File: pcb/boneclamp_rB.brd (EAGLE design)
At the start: 160 x 100 mm, 70 parts, among them IC1 24C, U1 AD8032ARZ-REEL7, U2 LT1964ES5-5TRMPBF, U4 TLV70245DBVT, U7 AD7682BCPZ, U8 TPS63700DRCT, U9 ADA4841-2YRZ

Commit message: Minor fixed to EEPROM circuit and ADC VREF buffer. Stephano, don't kill me.
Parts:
- removed S1: SWS002, smd-special:SMS-002
- removed SJ5: (no value), jumper:SJ
- added C2: 0.1uF, rcl:C0805
- added JP1: (no value), jumper:JP1
- added S2: SWS003, smd-special:SMS-003
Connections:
- net N$12 renamed ADC_CNV
- net AGND: now also C2.2
- net DGND: now also S2.4, S2.5, S2.6; no longer S1.3, S1.4
- net N$14: now also S2.1; no longer R8.1, S1.1
- net N$18: now also R8.1, S2.2; no longer S1.2
- net N$19: now also S2.3
- net N$21: now also JP1.2; no longer SJ5.1
- net N$22: now also JP1.1; no longer SJ5.2
- net VDD: now also C2.1
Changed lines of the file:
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@@
 <element name="SJ4" library="jumper" package="SJ" value="" x="25.4" y="58.42" rot="R90"/>
 <element name="IC1" library="on-semiconductor-01" package="SO-08" value="24C" x="25.4" y="27.94"/>
-<element name="S1" library="smd-special" package="SMS-002" value="SWS002" x="15.24" y="41.91"/>
 <element name="C22" library="rcl" package="C0603" value="0.1uF" x="12.7" y="24.13"/>
 <element name="R6" library="rcl" package="R0603" value="5.6k" x="12.7" y="20.32"/>
@@
 <element name="R10" library="rcl" package="R0603" value="5.6k" x="12.7" y="0"/>
 <element name="R11" library="rcl" package="R0603" value="10k" x="12.7" y="-5.08"/>
-<element name="SJ5" library="jumper" package="SJ" value="" x="12.7" y="-11.43"/>
 <element name="U$42" library="analog-devices-02" package="MO-153-AB" value="AD5686" x="17.78" y="60.96"/>
 <element name="U7" library="analog-devices-02" package="QFN50P400X400X100-21N" value="AD7682BCPZ" x="36.83" y="60.96">
@@
 <element name="SJ7" library="jumper" package="SJ" value="" x="-111.76" y="-334.01"/>
 <element name="SJ8" library="jumper" package="SJ" value="" x="-111.76" y="-339.09"/>
+<element name="JP1" library="jumper" package="JP1" value="" x="-118.11" y="-336.55"/>
+<element name="S2" library="smd-special" package="SMS-003" value="SWS003" x="-114.3" y="-346.71"/>
+<element name="C2" library="rcl" package="C0805" value="0.1uF" x="-119.38" y="-355.6"/>
 </elements>
 <signals>
@@
 <contactref element="U7" pad="20"/>
 <contactref element="U1" pad="8"/>
+<contactref element="C2" pad="1"/>
+<wire x1="-108.0262" y1="-302.895" x2="-120.33" y2="-355.6" width="0" layer="19" extent="1-1"/>
 <wire x1="-84.77" y1="-285.75" x2="-108.0262" y2="-302.895" width="0" layer="19" extent="1-1"/>
 <wire x1="-84.77" y1="-236.22" x2="-84.77" y2="-285.75" width="0" layer="19" extent="1-1"/>
@@
 <contactref element="U$42" pad="9"/>
 <contactref element="U$42" pad="16"/>
+<contactref element="C2" pad="2"/>
 <wire x1="-82.87" y1="-177.8" x2="-83.7692" y2="-167.9702" width="0" layer="19" extent="1-1"/>
 <wire x1="-82.87" y1="-184.15" x2="-82.87" y2="-177.8" width="0" layer="19" extent="1-1"/>
@@
 <wire x1="-110.81" y1="-314.96" x2="-112.9538" y2="-306.705" width="0" layer="19" extent="1-1"/>
 <wire x1="-110.91" y1="-327.66" x2="-110.81" y2="-314.96" width="0" layer="19" extent="1-1"/>
+<wire x1="-118.43" y1="-355.6" x2="-110.91" y2="-327.66" width="0" layer="19" extent="1-1"/>
 <wire x1="1.905" y1="19.05" x2="-81.0768" y2="-61.468" width="0" layer="19" extent="1-1"/>
 <wire x1="4.445" y1="19.05" x2="1.905" y2="19.05" width="0" layer="19" extent="1-1"/>
@@
 <contactref element="C22" pad="2"/>
 <contactref element="IC1" pad="4"/>
-<contactref element="S1" pad="3"/>
-<contactref element="S1" pad="4"/>
-<wire x1="25.4" y1="59.182" x2="50.165" y2="74.93" width="0" layer="19" extent="1-1"/>
-<wire x1="16.51" y1="46.4058" x2="25.4" y2="59.182" width="0" layer="19" extent="1-1"/>
-<wire x1="13.97" y1="46.4058" x2="16.51" y2="46.4058" width="0" layer="19" extent="1-1"/>
-<wire x1="13.55" y1="24.13" x2="13.97" y2="46.4058" width="0" layer="19" extent="1-1"/>
+<contactref element="S2" pad="5"/>
+<contactref element="S2" pad="6"/>
+<contactref element="S2" pad="4"/>
+<wire x1="-114.3" y1="-342.2142" x2="-116.84" y2="-342.2142" width="0" layer="19" extent="1-1"/>
+<wire x1="-111.76" y1="-342.2142" x2="-114.3" y2="-342.2142" width="0" layer="19" extent="1-1"/>
+<wire x1="13.55" y1="24.13" x2="-111.76" y2="-342.2142" width="0" layer="19" extent="1-1"/>
 <wire x1="27.305" y1="25.34" x2="13.55" y2="24.13" width="0" layer="19" extent="1-1"/>
+<wire x1="25.4" y1="59.182" x2="27.305" y2="25.34" width="0" layer="19" extent="1-1"/>
+<wire x1="50.165" y1="74.93" x2="25.4" y2="59.182" width="0" layer="19" extent="1-1"/>
 </signal>
 <signal name="VSS">
@@
 </signal>
 <signal name="N$14">
-<contactref element="S1" pad="1"/>
 <contactref element="IC1" pad="1"/>
 <contactref element="R7" pad="1"/>
-<contactref element="R8" pad="1"/>
-<wire x1="11.85" y1="15.24" x2="11.85" y2="10.16" width="0" layer="19" extent="1-1"/>
-<wire x1="13.97" y1="37.4142" x2="11.85" y2="15.24" width="0" layer="19" extent="1-1"/>
-<wire x1="23.495" y1="25.34" x2="13.97" y2="37.4142" width="0" layer="19" extent="1-1"/>
+<contactref element="S2" pad="1"/>
+<wire x1="11.85" y1="15.24" x2="-116.84" y2="-351.2058" width="0" layer="19" extent="1-1"/>
+<wire x1="23.495" y1="25.34" x2="11.85" y2="15.24" width="0" layer="19" extent="1-1"/>
 </signal>
 <signal name="N$18">
 <contactref element="IC1" pad="2"/>
-<contactref element="S1" pad="2"/>
-<wire x1="24.765" y1="25.34" x2="16.51" y2="37.4142" width="0" layer="19" extent="1-1"/>
+<contactref element="S2" pad="2"/>
+<contactref element="R8" pad="1"/>
+<wire x1="11.85" y1="10.16" x2="-114.3" y2="-351.2058" width="0" layer="19" extent="1-1"/>
+<wire x1="24.765" y1="25.34" x2="11.85" y2="10.16" width="0" layer="19" extent="1-1"/>
 </signal>
 <signal name="N$19">
 <contactref element="IC1" pad="3"/>
 <contactref element="R9" pad="1"/>
+<contactref element="S2" pad="3"/>
+<wire x1="11.85" y1="5.08" x2="-111.76" y2="-351.2058" width="0" layer="19" extent="1-1"/>
 <wire x1="26.035" y1="25.34" x2="11.85" y2="5.08" width="0" layer="19" extent="1-1"/>
 </signal>
 <signal name="N$22">
 <contactref element="R11" pad="1"/>
-<contactref element="SJ5" pad="2"/>
-<wire x1="11.85" y1="-5.08" x2="13.462" y2="-11.43" width="0" layer="19" extent="1-1"/>
+<contactref element="JP1" pad="1"/>
+<wire x1="11.85" y1="-5.08" x2="-118.11" y2="-337.82" width="0" layer="19" extent="1-1"/>
 </signal>
 <signal name="N$21">
-<contactref element="SJ5" pad="1"/>
 <contactref element="IC1" pad="7"/>
-<wire x1="24.765" y1="30.54" x2="11.938" y2="-11.43" width="0" layer="19" extent="1-1"/>
+<contactref element="JP1" pad="2"/>
+<wire x1="24.765" y1="30.54" x2="-118.11" y2="-335.28" width="0" layer="19" extent="1-1"/>
 </signal>
 <signal name="SYS_5V">
@@
 <wire x1="38.608" y1="60.452" x2="-110.998" y2="-334.01" width="0" layer="19" extent="1-1"/>
 </signal>
-<signal name="N$12">
+<signal name="ADC_CNV">
 <contactref element="U7" pad="11"/>
 </signal>

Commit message: Minor edit
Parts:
- added TP7: TPB1,27, testpad:B1,27
- moved JP1 420.5 mm to (127.0, 5.08)
- moved S2 408.9 mm to (114.3, -7.62)
- moved TP6 316.4 mm to (157.5, -10.2)
- moved TP5 315.0 mm to (152.4, -1.27)
- moved C22 127.0 mm to (139.7, 24.1)
- moved R10 127.0 mm to (139.7, 0.00)
- moved R11 127.0 mm to (139.7, -5.08)
- moved R6 127.0 mm to (139.7, 20.3)
- moved R7 127.0 mm to (139.7, 15.2)
- moved R8 127.0 mm to (139.7, 10.2)
- moved R9 127.0 mm to (139.7, 5.08)
- moved IC1 95.7 mm to (120.7, 19.1)
- moved C12 40.9 mm to (-47.0, -261.6)
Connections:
- net I2C2_SDA: now also TP7.TP

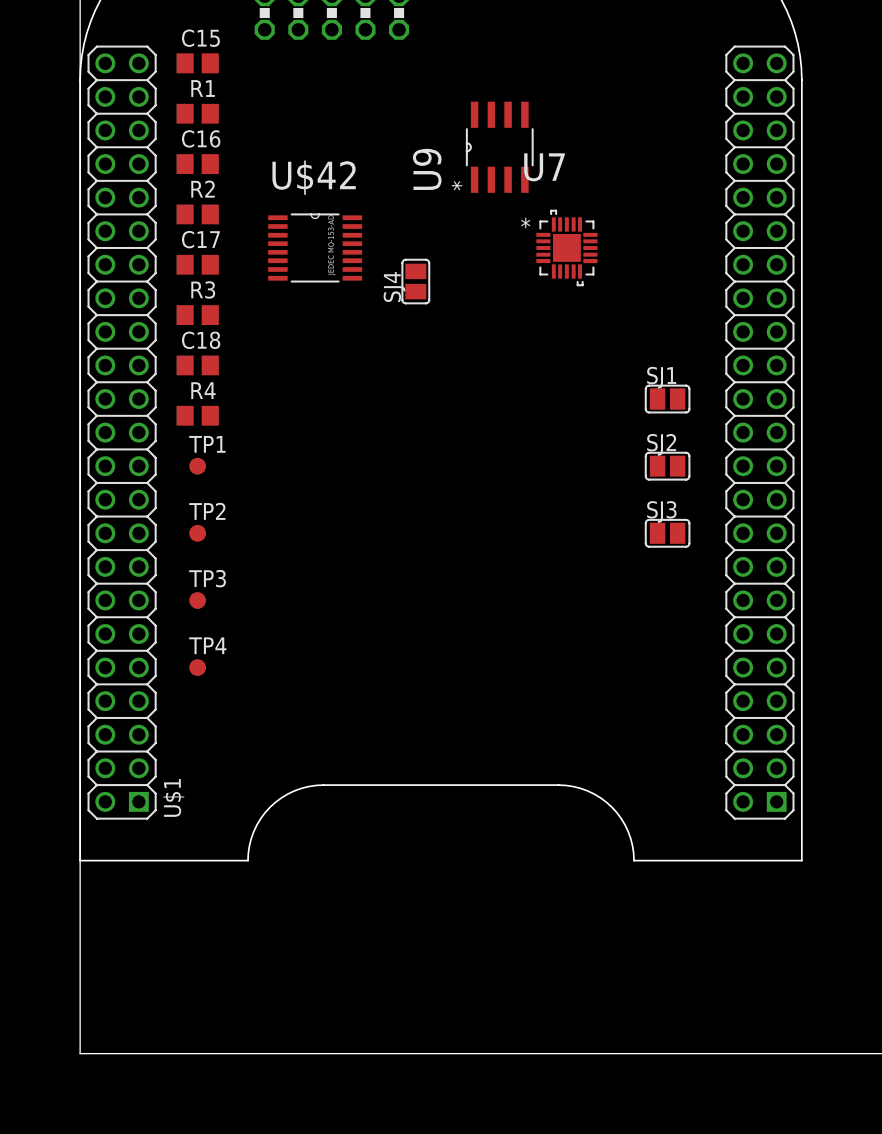
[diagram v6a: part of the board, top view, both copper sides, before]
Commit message: Added p6 to the schematic of the BB, update the BC shematic and board
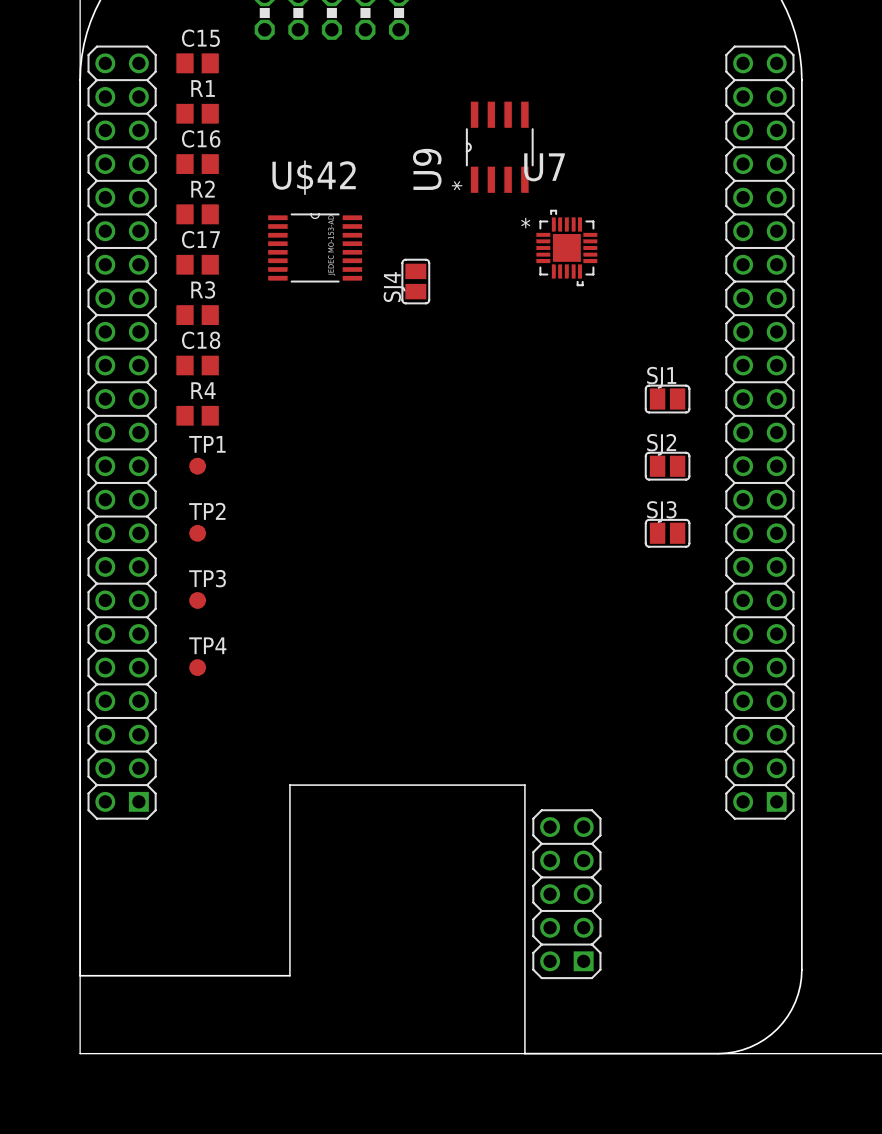
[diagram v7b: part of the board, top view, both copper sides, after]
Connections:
- new net BAT_SENSE: U$1.95
- new net BL_IN: U$1.97
- new net BL_OUT: U$1.100
- new net BL_SINK1: U$1.101
- new net BL_SINK2: U$1.102
- new net GND: U$1.1, U$1.2, U$1.47, U$1.48, U$1.89, U$1.91
- net AGND: no longer U$1.1, U$1.2, U$1.47, U$1.48, U$1.89, U$1.91
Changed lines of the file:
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@@
 </signal>
 <signal name="AGND">
-<contactref element="U$1" pad="47"/>
-<contactref element="U$1" pad="48"/>
-<contactref element="U$1" pad="89"/>
-<contactref element="U$1" pad="91"/>
-<contactref element="U$1" pad="1"/>
-<contactref element="U$1" pad="2"/>
 <contactref element="U$1" pad="90"/>
 <contactref element="R4" pad="1"/>
@@
 <wire x1="8.89" y1="29.21" x2="14.9606" y2="61.9252" width="0" layer="19" extent="1-1"/>
 </signal>
+<signal name="GND">
+<contactref element="U$1" pad="47"/>
+<contactref element="U$1" pad="48"/>
+<contactref element="U$1" pad="89"/>
+<contactref element="U$1" pad="91"/>
+<contactref element="U$1" pad="1"/>
+<contactref element="U$1" pad="2"/>
+<wire x1="52.705" y1="72.39" x2="52.705" y2="74.93" width="0" layer="19" extent="1-1"/>
+<wire x1="52.705" y1="19.05" x2="52.705" y2="72.39" width="0" layer="19" extent="1-1"/>
+<wire x1="50.165" y1="19.05" x2="52.705" y2="19.05" width="0" layer="19" extent="1-1"/>
+<wire x1="4.445" y1="19.05" x2="50.165" y2="19.05" width="0" layer="19" extent="1-1"/>
+<wire x1="1.905" y1="19.05" x2="4.445" y2="19.05" width="0" layer="19" extent="1-1"/>
+</signal>
+<signal name="BAT_SENSE">
+<contactref element="U$1" pad="95"/>
+</signal>
+<signal name="BL_OUT">
+<contactref element="U$1" pad="100"/>
+</signal>
+<signal name="BL_IN">
+<contactref element="U$1" pad="97"/>
+</signal>
+<signal name="BL_SINK1">
+<contactref element="U$1" pad="101"/>
+</signal>
+<signal name="BL_SINK2">
+<contactref element="U$1" pad="102"/>
+</signal>
 </signals>

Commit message: Added Ground and power plane to pcb. Power plane will need to be split into primarly VDD and then a bit at the front of the board for VSS. VDD and VSS planes should not overlap in the Z direction.
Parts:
- removed U$27: (no value), boneclamp:DO-219AB
- added C3: 10uF, rcl:C0805
- added D1: (no value), boneclamp:DO-219AB
- C23, C24, C26, C27, C29, C30, C31, C32, C33, C34, C35, C5, C6, C7, C8, C9: device rcl:C0805 -> rcl:C0603
- R12, R13, R5: device resistor:R0805 -> rcl:R0603
- moved U8 25.0 mm to (-61.0, -73.7)
- moved C23 23.7 mm to (-61.0, -76.2)
- moved R5 23.4 mm to (-61.0, -68.6), turned to 90 degrees
- moved C27 17.1 mm to (-71.1, -77.5)
- moved C24 15.5 mm to (-68.6, -76.2)
- moved C26 15.3 mm to (-72.4, -73.7)
- renumbered U$28 to L1
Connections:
- net AGND: now also C3.2
- net N$27: now also D1.P$1; no longer U$27.P$1
- net VDD: now also C3.1
- net _VSS: now also D1.P$2; no longer U$27.P$2
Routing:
- added copper zone on layer 15, net AGND
- added copper zone on layer 2, net VDD
